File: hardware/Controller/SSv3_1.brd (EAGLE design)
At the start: 127 x 100.1 mm, 197 parts, among them Q1 20.000_MHZ, Q2 200mA/50V, X1 PN61729-S, X2 SCAN_LED, X3 RJ45-6L-B, X4 C-GRID-06-74099

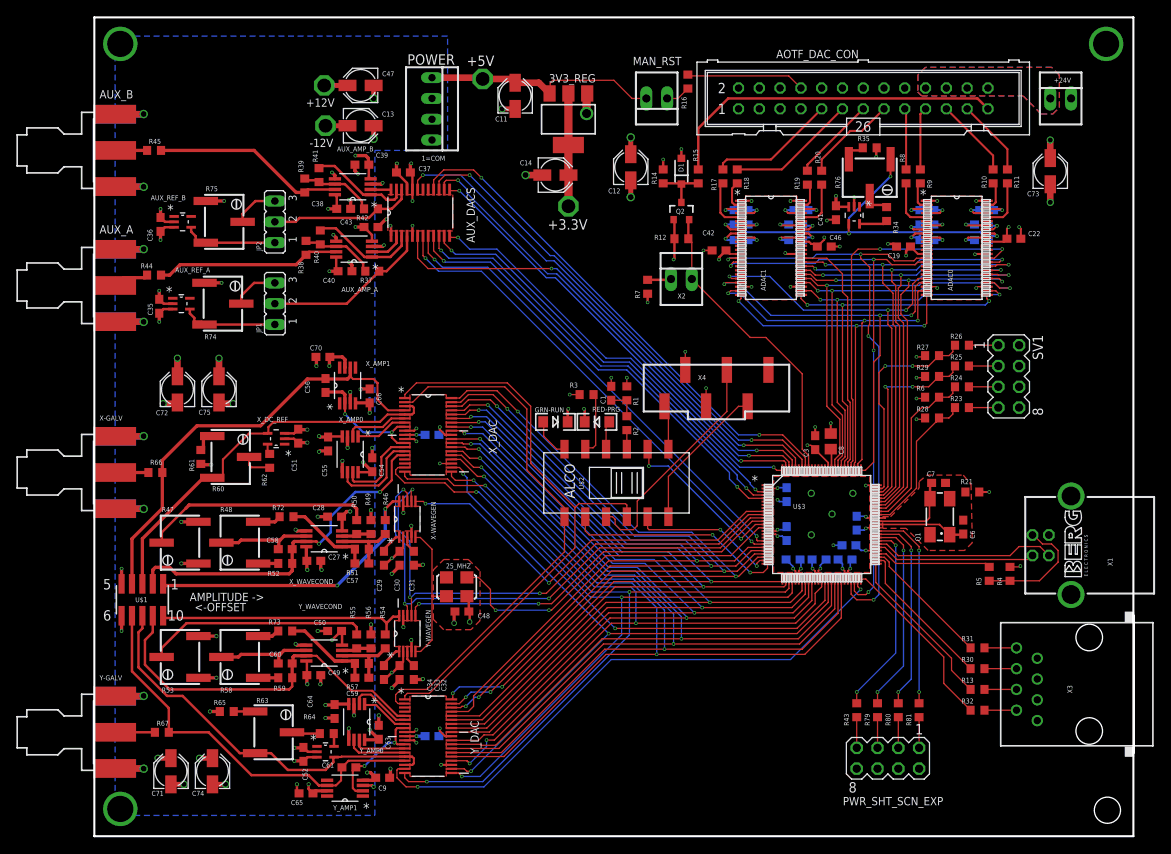
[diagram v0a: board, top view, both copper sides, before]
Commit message: Working on BOM and tidying up wire stubs on board
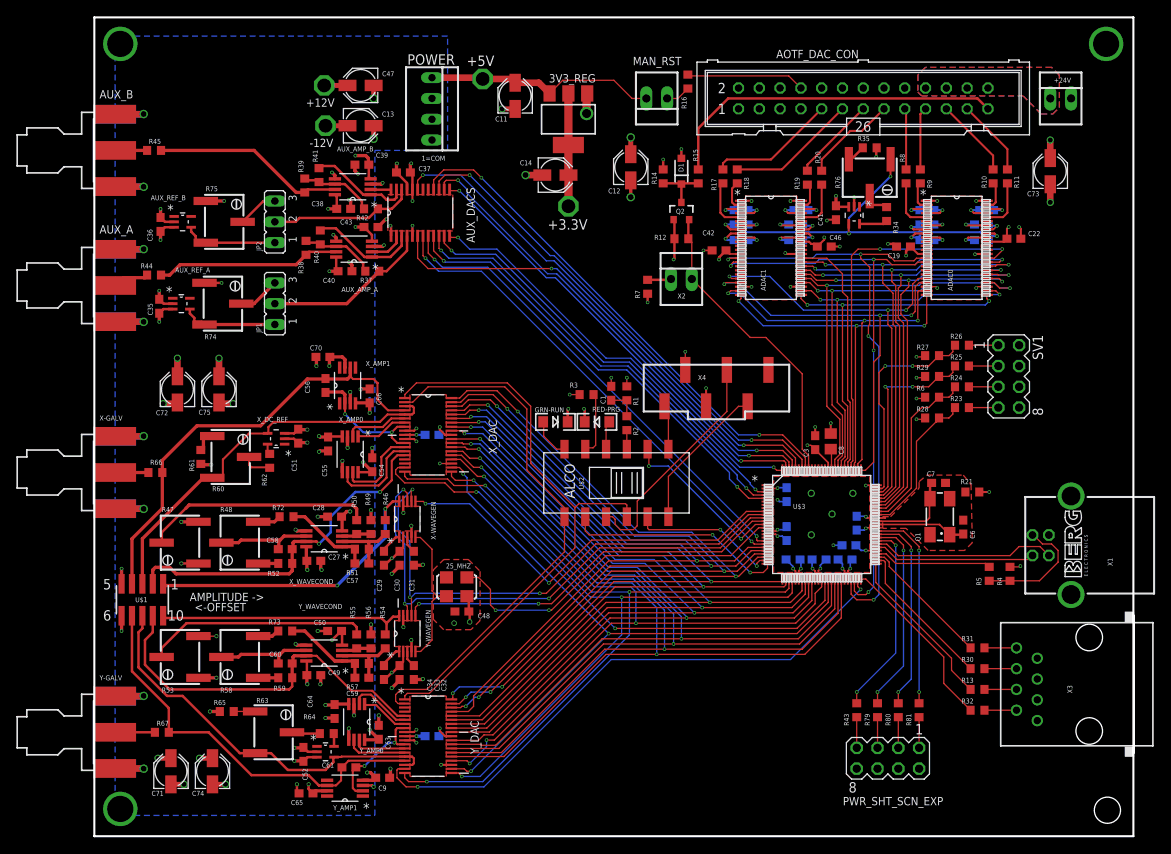
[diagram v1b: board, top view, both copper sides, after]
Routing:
- net AGND: track 266.6 -> 265.2 mm
- net +5V: track 29.3 -> 28.6 mm
- net N$55: track 2.91 -> 2.28 mm
- net N$86: track 5.57 -> 4.99 mm
- net N$53: track 5.73 -> 5.15 mm
